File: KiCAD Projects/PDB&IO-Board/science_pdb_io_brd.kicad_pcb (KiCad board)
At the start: 2 copper layers, 146.1 x 94 mm, 41 parts, among them P1 PWR_IN, P11 ENCODER_1, P13 LIMIT1_IN, P14 LIMIT2_IN, P15 LIMIT3_IN, P16 ENCODER_3, P17 MOTOR1_PWM, P18 MOTOR2_PWM, P19 MOTOR3_PWM, P2 RPI_HEADER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

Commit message: Power Layout Mostly Done
Just needs ground planes and a few tweaks.
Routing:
- net +3V3: track 13.9 -> 406.2 mm, vias 0 -> 2
- net +5V: track 0.00 -> 282.5 mm, vias 0 -> 2
- net /CAM_TRIG: track 154.6 -> 154.7 mm, vias 0 -> 2
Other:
- net class Low Power added: clearance 0.2, trace_width 1.016, via_dia 1.27, via_drill 0.508
- net class Power added: clearance 0.2, trace_width 1.27, via_dia 1.524, via_drill 0.762

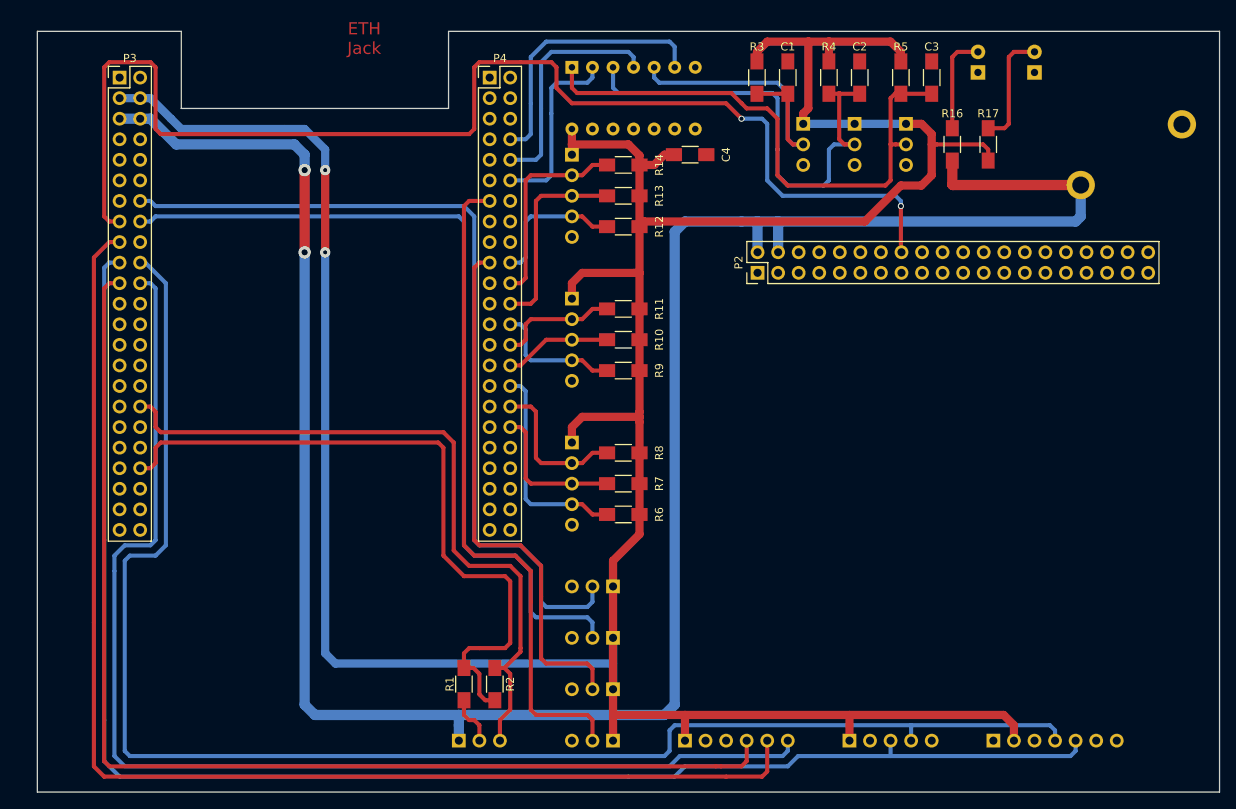
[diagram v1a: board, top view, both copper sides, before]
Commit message: Main Board Almost Finished
Needs via stitching between ground planes under BeagleBone, then
everything should be connected and ready to go!
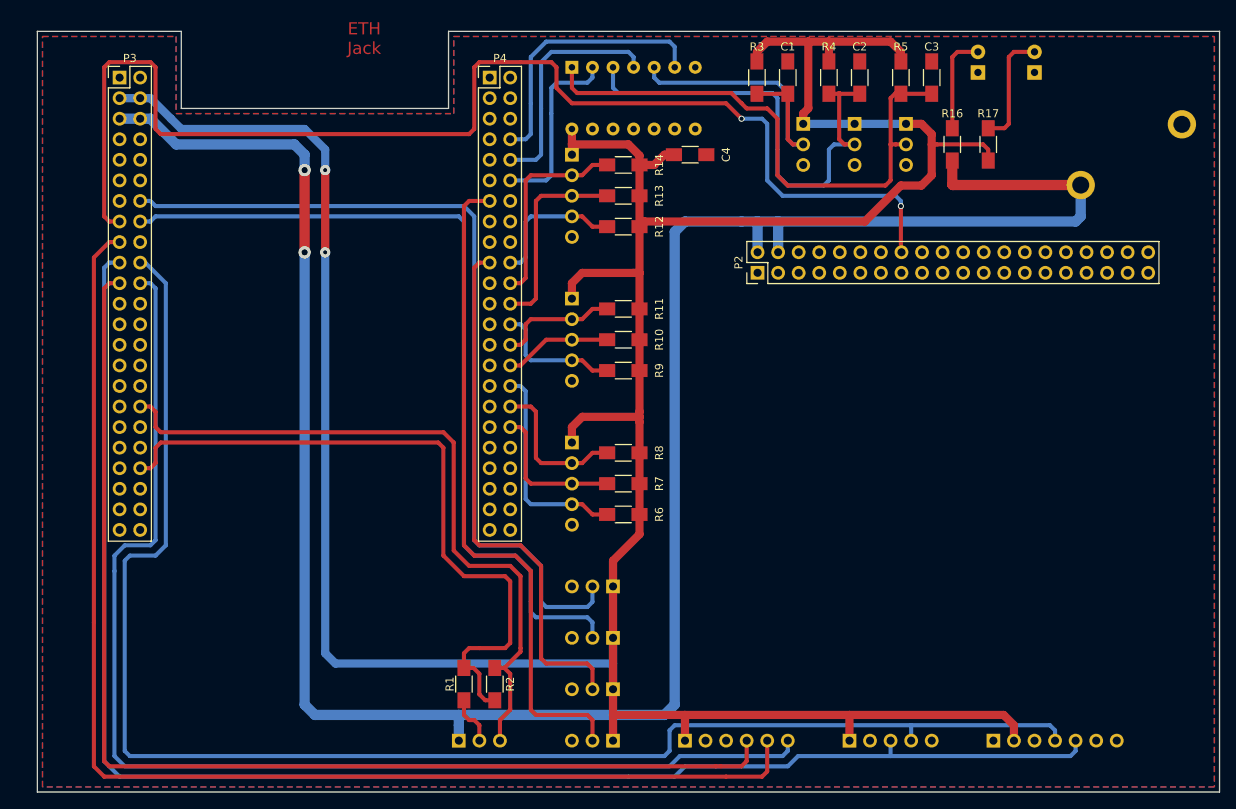
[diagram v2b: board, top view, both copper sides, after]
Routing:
- added copper zone on B.Cu, net GNDD
- added copper zone on F.Cu, net GNDD
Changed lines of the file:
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@@
   (general
     (links 120)
-    (no_connects 36)
+    (no_connects 2)
     (area 36.754999 21.514999 182.955001 115.645001)
     (thickness 1.6)
@@
     (add_net /SPI_DO)
     (add_net GNDA)
-    (add_net GNDD)
     (add_net "Net-(D2-Pad2)")
     (add_net "Net-(D3-Pad2)")
@@
     (uvia_drill 0.1)
     (add_net +3V3)
+    (add_net GNDD)
   )
   (net_class Power ""
@@
   (segment (start 88.9 106.045) (end 88.9 107.315) (width 1.27) (layer B.Cu) (net 55))
   (segment (start 88.9 107.315) (end 88.9 109.22) (width 1.27) (layer B.Cu) (net 55))
-  (segment (start 46.99 32.385) (end 49.53 32.385) (width 1.27) (layer B.Cu) (net 55) (status C00000))
-  (segment (start 49.53 32.385) (end 50.8 32.385) (width 1.27) (layer B.Cu) (net 55) (status 400000))
+  (segment (start 46.99 32.385) (end 49.53 32.385) (width 1.27) (layer B.Cu) (net 55))
+  (segment (start 49.53 32.385) (end 50.8 32.385) (width 1.27) (layer B.Cu) (net 55))
   (segment (start 50.8 32.385) (end 53.975 35.56) (width 1.27) (layer B.Cu) (net 55))
   (segment (start 53.975 35.56) (end 68.58 35.56) (width 1.27) (layer B.Cu) (net 55))
@@
   (segment (start 153.67 35.56) (end 147.955 35.56) (width 0.508) (layer F.Cu) (net 73))
   (segment (start 154.305 36.195) (end 154.305 37.56) (width 0.508) (layer F.Cu) (net 73))
-  (segment (start 144.145 33.02) (end 146.05 33.02) (width 1.016) (layer F.Cu) (net 73) (status 400000))
-  (segment (start 139.065 45.085) (end 111.855 45.085) (width 1.016) (layer F.Cu) (net 73) (status 800000))
+  (segment (start 144.145 33.02) (end 146.05 33.02) (width 1.016) (layer F.Cu) (net 73))
+  (segment (start 139.065 45.085) (end 111.855 45.085) (width 1.016) (layer F.Cu) (net 73))
   (segment (start 143.51 40.64) (end 139.065 45.085) (width 1.016) (layer F.Cu) (net 73))
   (segment (start 146.05 40.64) (end 143.51 40.64) (width 1.016) (layer F.Cu) (net 73))
@@
   (segment (start 147.32 35.56) (end 147.32 39.37) (width 1.016) (layer F.Cu) (net 73))
   (segment (start 146.05 33.02) (end 147.32 34.29) (width 1.016) (layer F.Cu) (net 73))
-  (segment (start 111.855 45.085) (end 111.22 45.72) (width 1.016) (layer F.Cu) (net 73) (status C00000))
-  (segment (start 49.53 29.845) (end 50.8 29.845) (width 1.016) (layer B.Cu) (net 73) (status 400000))
+  (segment (start 111.855 45.085) (end 111.22 45.72) (width 1.016) (layer F.Cu) (net 73))
+  (segment (start 49.53 29.845) (end 50.8 29.845) (width 1.016) (layer B.Cu) (net 73))
   (segment (start 69.85 33.655) (end 72.39 36.195) (width 1.016) (layer B.Cu) (net 73))
   (segment (start 72.39 36.195) (end 72.39 38.735) (width 1.016) (layer B.Cu) (net 73))
@@
   (segment (start 54.61 33.655) (end 67.31 33.655) (width 1.016) (layer B.Cu) (net 73))
   (segment (start 67.31 33.655) (end 69.85 33.655) (width 1.016) (layer B.Cu) (net 73))
-  (segment (start 107.95 99.695) (end 107.95 102.87) (width 1.016) (layer B.Cu) (net 73) (status 800000))
-  (segment (start 107.95 99.695) (end 107.95 96.52) (width 1.016) (layer B.Cu) (net 73) (status 800000))
-  (segment (start 46.99 29.845) (end 49.53 29.845) (width 1.016) (layer B.Cu) (net 73) (status C00000))
+  (segment (start 107.95 99.695) (end 107.95 102.87) (width 1.016) (layer B.Cu) (net 73))
+  (segment (start 107.95 99.695) (end 107.95 96.52) (width 1.016) (layer B.Cu) (net 73))
+  (segment (start 46.99 29.845) (end 49.53 29.845) (width 1.016) (layer B.Cu) (net 73))
   (segment (start 137.16 106.045) (end 156.21 106.045) (width 1.016) (layer F.Cu) (net 73))
-  (segment (start 157.48 107.315) (end 157.48 109.22) (width 1.016) (layer F.Cu) (net 73) (status 800000))
+  (segment (start 157.48 107.315) (end 157.48 109.22) (width 1.016) (layer F.Cu) (net 73))
   (segment (start 156.21 106.045) (end 157.48 107.315) (width 1.016) (layer F.Cu) (net 73))
   (segment (start 116.84 106.045) (end 137.16 106.045) (width 1.016) (layer F.Cu) (net 73))
-  (segment (start 137.16 106.045) (end 137.16 109.22) (width 1.016) (layer F.Cu) (net 73) (status 800000))
+  (segment (start 137.16 106.045) (end 137.16 109.22) (width 1.016) (layer F.Cu) (net 73))
   (segment (start 107.95 106.045) (end 116.84 106.045) (width 1.016) (layer F.Cu) (net 73))
-  (segment (start 116.84 106.045) (end 116.84 109.22) (width 1.016) (layer F.Cu) (net 73) (status 800000))
+  (segment (start 116.84 106.045) (end 116.84 109.22) (width 1.016) (layer F.Cu) (net 73))
   (segment (start 132.08 22.86) (end 132.08 31.115) (width 1.016) (layer F.Cu) (net 73))
   (segment (start 131.445 31.75) (end 131.445 33.02) (width 1.016) (layer F.Cu) (net 73))
@@
   (segment (start 156.845 33.02) (end 156.845 24.765) (width 0.508) (layer F.Cu) (net 126))
   (segment (start 156.305 33.56) (end 156.845 33.02) (width 0.508) (layer F.Cu) (net 126))
-  (segment (start 143.51 43.18) (end 143.51 48.8061) (width 0.508) (layer F.Cu) (net 127) (status 800000))
-  (segment (start 143.51 48.8061) (end 143.5862 48.8823) (width 0.508) (layer F.Cu) (net 127) (status C00000))
+  (segment (start 143.51 43.18) (end 143.51 48.8061) (width 0.508) (layer F.Cu) (net 127))
+  (segment (start 143.51 48.8061) (end 143.5862 48.8823) (width 0.508) (layer F.Cu) (net 127))
   (segment (start 121.92 30.48) (end 123.825 32.385) (width 0.508) (layer F.Cu) (net 127))
   (segment (start 45.72 45.085) (end 45.085 44.45) (width 0.508) (layer F.Cu) (net 127))
@@
   (segment (start 123.825 32.385) (end 126.365 32.385) (width 0.508) (layer B.Cu) (net 127))
   (via (at 123.825 32.385) (size 0.762) (drill 0.508) (layers F.Cu B.Cu) (net 127))
+  (zone (net 69) (net_name GNDD) (layer F.Cu) (hatch edge 0.508)
+    (connect_pads (clearance 0.508))
+    (min_thickness 0.254)
+    (fill yes (arc_segments 16) (thermal_gap 0.508) (thermal_bridge_width 0.508))
+    (polygon
+      (pts
+        (xy 53.975 31.75) (xy 88.265 31.75) (xy 88.265 22.225) (xy 182.245 22.225) (xy 182.245 114.935)
+        (xy 37.465 114.935) (xy 37.465 22.225) (xy 53.975 22.225)
+      )
+    )
+  )
+  (zone (net 69) (net_name GNDD) (layer B.Cu) (hatch edge 0.508)
+    (connect_pads (clearance 0.508))
+    (min_thickness 0.254)
+    (fill yes (arc_segments 16) (thermal_gap 0.508) (thermal_bridge_width 0.508))
+    (polygon
+      (pts
+        (xy 53.975 31.75) (xy 88.265 31.75) (xy 88.265 22.225) (xy 182.245 22.225) (xy 182.245 114.935)
+        (xy 37.465 114.935) (xy 37.465 22.225) (xy 53.975 22.225)
+      )
+    )
+  )
 )

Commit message: Finished Getting Main Board Routed!
Everything's connected together as it needs to be. Some minor tweaks,
then off to revision!
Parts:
- added REF**: VIA-0.4, .pretty:VIA-0.04, F.Cu at (61.6, 67.9)
- added REF**: VIA-0.4, .pretty:VIA-0.04, F.Cu at (80.6, 67.9)
- added REF**: VIA-0.4, .pretty:VIA-0.04, F.Cu at (149.9, 74.9)
- added REF**: VIA-0.4, .pretty:VIA-0.04, F.Cu at (80.6, 75.6)
- added REF**: VIA-0.4, .pretty:VIA-0.04, F.Cu at (61.6, 75.6)
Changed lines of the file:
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@@
 (kicad_pcb (version 4) (host pcbnew 4.0.3-stable)
   (general
-    (links 120)
+    (links 123)
     (no_connects 2)
     (area 36.754999 21.514999 182.955001 115.645001)
@@
     (tracks 456)
     (zones 0)
-    (modules 41)
+    (modules 46)
     (nets 130)
   )
@@
     (mod_text_width 0.15)
     (pad_size 1.524 1.524)
-    (pad_drill 0.762)
+    (pad_drill 1.016)
     (pad_to_mask_clearance 0.2)
     (aux_axis_origin 0 0)
@@
       (net 55 +5V))
   )
+  (module .pretty:VIA-0.04 (layer F.Cu)
+    (at 61.595 67.945)
+    (fp_text reference REF** (at 0 1.143) (layer F.SilkS) hide
+      (effects (font (size 0.25 0.25) (thickness 0.05)))
+    )
+    (fp_text value VIA-0.4 (at 0 -1.143) (layer F.Fab) hide
+      (effects (font (size 0.25 0.25) (thickness 0.05)))
+    )
+    (pad 1 thru_hole circle (at 0 0) (size 1.524 1.524) (drill 1.016) (layers *.Cu)
+      (net 69 GNDD) (zone_connect 2))
+  )
+  (module .pretty:VIA-0.04 (layer F.Cu)
+    (at 80.645 67.945)
+    (fp_text reference REF** (at 0 1.143) (layer F.SilkS) hide
+      (effects (font (size 0.25 0.25) (thickness 0.05)))
+    )
+    (fp_text value VIA-0.4 (at 0 -1.143) (layer F.Fab) hide
+      (effects (font (size 0.25 0.25) (thickness 0.05)))
+    )
+    (pad 1 thru_hole circle (at 0 0) (size 1.524 1.524) (drill 1.016) (layers *.Cu)
+      (net 69 GNDD) (zone_connect 2))
+  )
+  (module .pretty:VIA-0.04 (layer F.Cu)
+    (at 149.86 74.93)
+    (fp_text reference REF** (at 0 1.143) (layer F.SilkS) hide
+      (effects (font (size 0.25 0.25) (thickness 0.05)))
+    )
+    (fp_text value VIA-0.4 (at 0 -1.143) (layer F.Fab) hide
+      (effects (font (size 0.25 0.25) (thickness 0.05)))
+    )
+    (pad 1 thru_hole circle (at 0 0) (size 1.524 1.524) (drill 1.016) (layers *.Cu)
+      (net 69 GNDD) (zone_connect 2))
+  )
+  (module .pretty:VIA-0.04 (layer F.Cu)
+    (at 80.645 75.565)
+    (fp_text reference REF** (at 0 1.143) (layer F.SilkS) hide
+      (effects (font (size 0.25 0.25) (thickness 0.05)))
+    )
+    (fp_text value VIA-0.4 (at 0 -1.143) (layer F.Fab) hide
+      (effects (font (size 0.25 0.25) (thickness 0.05)))
+    )
+    (pad 1 thru_hole circle (at 0 0) (size 1.524 1.524) (drill 1.016) (layers *.Cu)
+      (net 69 GNDD) (zone_connect 2))
+  )
+  (module .pretty:VIA-0.04 (layer F.Cu)
+    (at 61.595 75.565)
+    (fp_text reference REF** (at 0 1.143) (layer F.SilkS) hide
+      (effects (font (size 0.25 0.25) (thickness 0.05)))
+    )
+    (fp_text value VIA-0.4 (at 0 -1.143) (layer F.Fab) hide
+      (effects (font (size 0.25 0.25) (thickness 0.05)))
+    )
+    (pad 1 thru_hole circle (at 0 0) (size 1.524 1.524) (drill 1.016) (layers *.Cu)
+      (net 69 GNDD) (zone_connect 2))
+  )
   (gr_text "5V Power" (at 149.225 26.67) (layer B.SilkS)
